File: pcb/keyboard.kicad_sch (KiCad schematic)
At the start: 21 parts, among them SW1 SW_Push, SW10 RotaryEncoder_Switch, SW2 SW_Push, SW3 SW_Push, SW4 SW_Push, SW5 SW_Push, SW6 SW_Push, SW7 SW_Push, SW8 SW_Push, SW9 SW_Push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

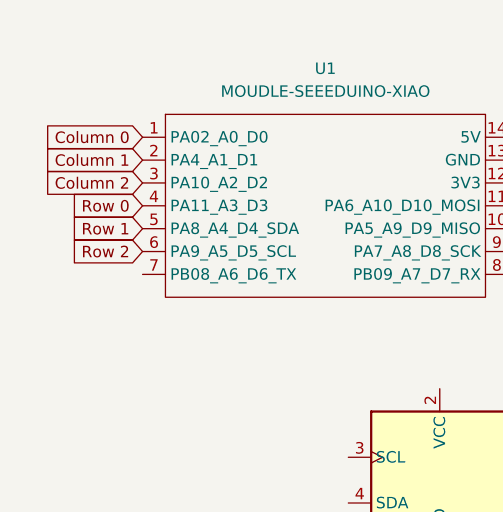
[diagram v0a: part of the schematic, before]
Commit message: connect switches to the microcontroller
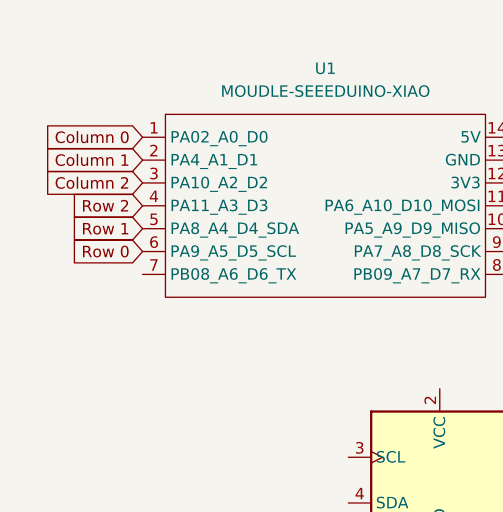
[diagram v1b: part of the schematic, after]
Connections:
- net Row 0: now also U1.6 (PA9_A5_D5_SCL); no longer U1.4 (PA11_A3_D3)
- net Row 2: now also U1.4 (PA11_A3_D3); no longer U1.6 (PA9_A5_D5_SCL)
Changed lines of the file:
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@@
 	(global_label "Row 2"
 		(shape input)
-		(at 30.48 50.8 180)
+		(at 30.48 45.72 180)
 		(fields_autoplaced yes)
 		(effects
@@
 		)
 		(property "Intersheetrefs" "${INTERSHEET_REFS}"
-			(at 21.5682 50.8 0)
+			(at 21.5682 45.72 0)
 			(hide yes)
 			(show_name no)
@@
 	(global_label "Row 0"
 		(shape input)
-		(at 30.48 45.72 180)
+		(at 30.48 50.8 180)
 		(fields_autoplaced yes)
 		(effects
@@
 		)
 		(property "Intersheetrefs" "${INTERSHEET_REFS}"
-			(at 21.5682 45.72 0)
+			(at 21.5682 50.8 0)
 			(hide yes)
 			(show_name no)

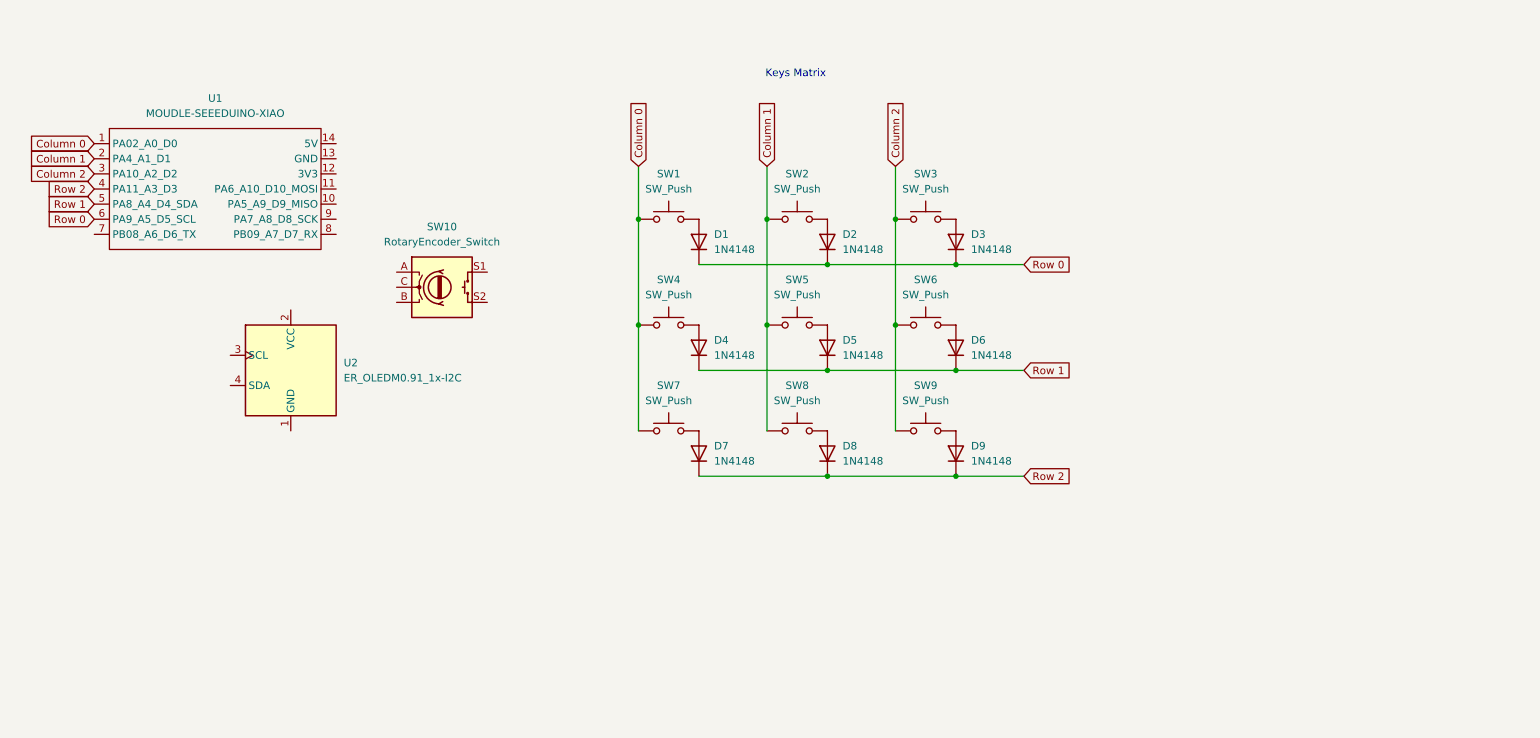
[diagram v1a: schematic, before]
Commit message: connect all components on schematic; remove invalid connections on pcb
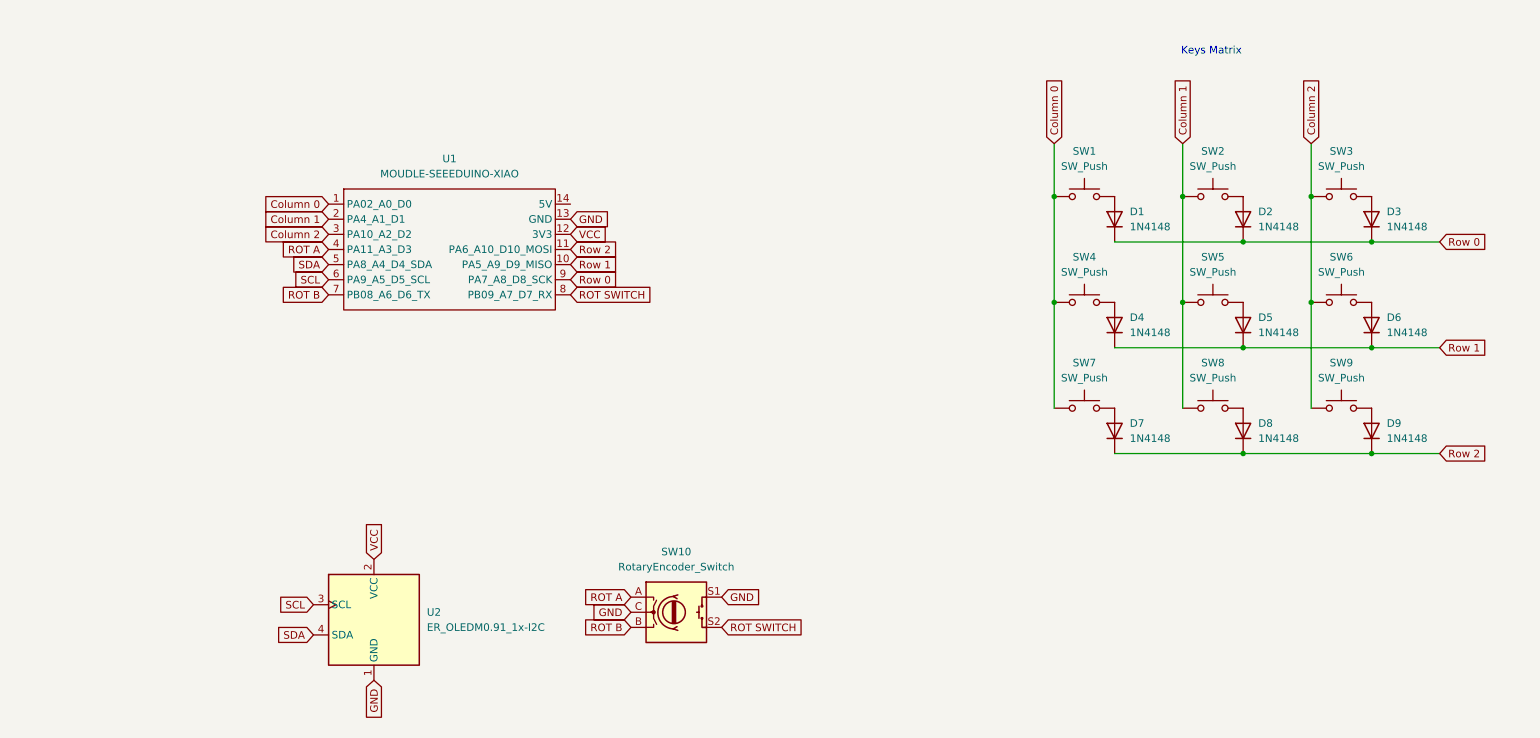
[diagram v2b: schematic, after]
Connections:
- net Row 0: now also U1.9 (PA7_A8_D8_SCK); no longer U1.6 (PA9_A5_D5_SCL)
- net Row 1: now also U1.10 (PA5_A9_D9_MISO); no longer U1.5 (PA8_A4_D4_SDA)
- net Row 2: now also U1.11 (PA6_A10_D10_MOSI); no longer U1.4 (PA11_A3_D3)
- net ROT A: now reaches SW10.A
- net ROT A: now also U1.4 (PA11_A3_D3)
- net ROT B: now reaches SW10.B
- net ROT B: now also U1.7 (PB08_A6_D6_TX)
- net GND: now reaches SW10.C
- net GND: now also SW10.S1, U1.13 (GND), U2.1 (GND)
- net ROT SWITCH: now reaches SW10.S2
- net ROT SWITCH: now also U1.8 (PB09_A7_D7_RX)
- net VCC: now reaches U2.2 (VCC)
- net VCC: now also U1.12 (3V3)
- net SCL: now reaches U2.3 (SCL)
- net SCL: now also U1.6 (PA9_A5_D5_SCL)
- net SDA: now reaches U2.4 (SDA)
- net SDA: now also U1.5 (PA8_A4_D4_SDA)
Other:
- moved on the sheet: D1, D2, D3, D4, D5, D6, D7, D8, D9, SW1, SW10, SW2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

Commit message: add rgb leds to schematic; update power labels; remove a switch and add rotary knob one to matrix instead
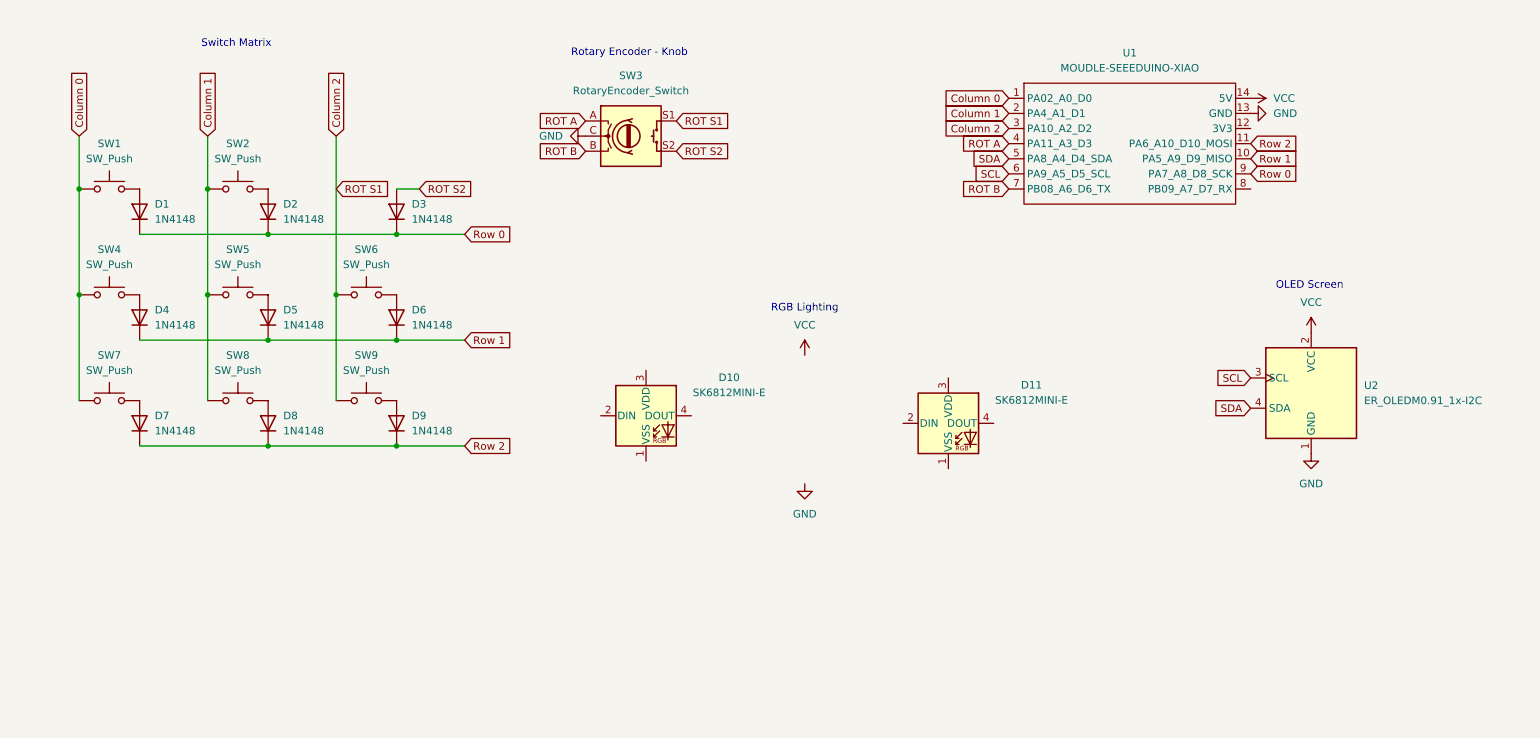
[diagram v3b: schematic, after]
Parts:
- removed SW3: SW_Push, Button_Switch_Keyboard:SW_Cherry_MX_1.00u_PCB, symbol Switch:SW_Push
- added D10, D11: SK6812MINI-E, footprints:SK6812MINI-E_fixed, symbol LED:SK6812MINI-E
- renumbered SW10 to SW3
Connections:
- net Column 2: now also SW3.S1
- net GND: no longer SW3.S1
- net VCC: now also U1.14 (5V); no longer U1.12 (3V3)
- net ROT S2: now reaches D3.2 (A)
- net ROT S2: now also SW3.S2
- net ROT SWITCH: no longer names the net of U1.8 (PB09_A7_D7_RX)
- net ROT SWITCH: no longer SW3.S2
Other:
- note added: "OLED Screen"
- note added: "RGB Lighting"
- note added: "Rotary Encoder - Knob"
- note added: "Switch Matrix"
- note removed: "Keys Matrix"
- moved on the sheet: D1, D2, D3, D4, D5, D6, D7, D8, D9, SW1, SW2, SW3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

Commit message: connect everything on the schematic
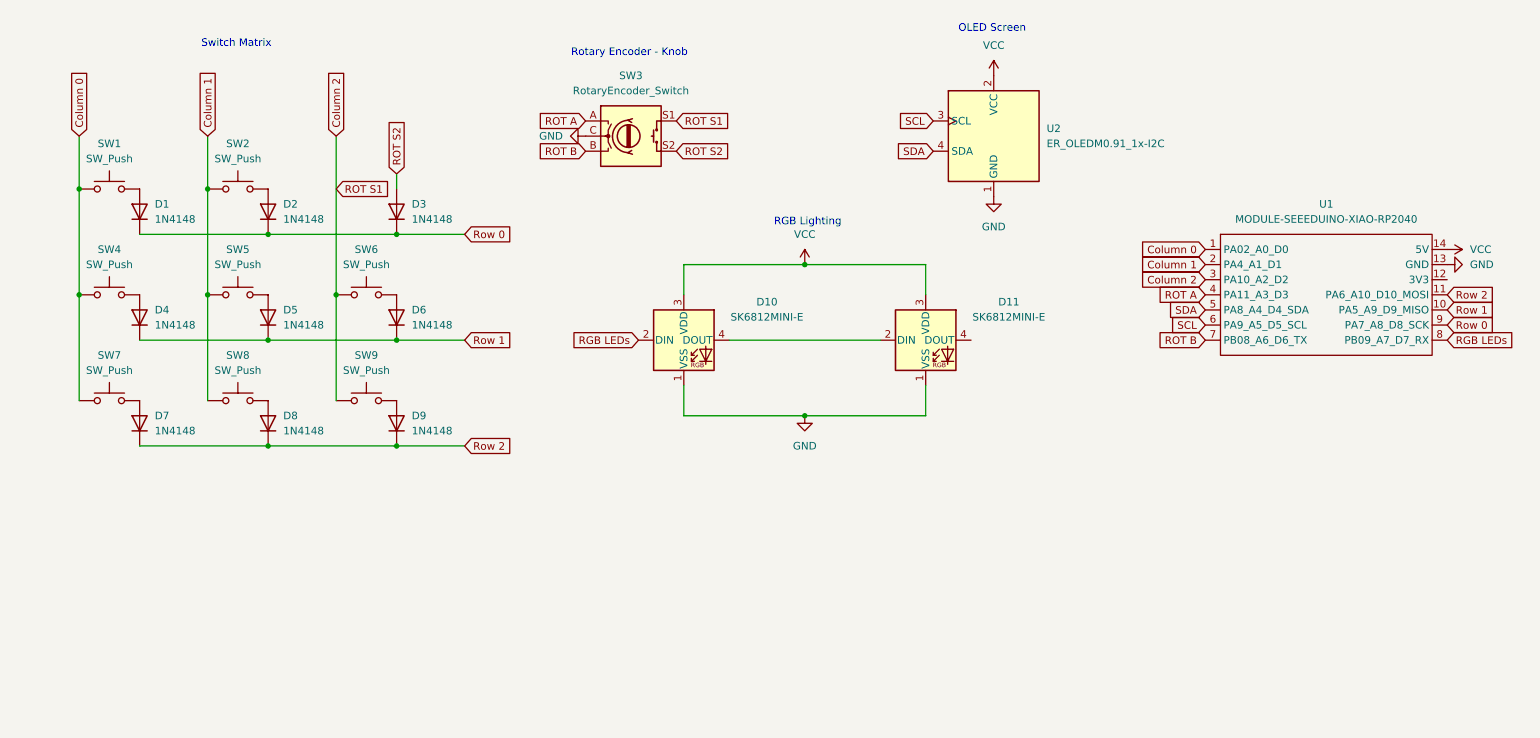
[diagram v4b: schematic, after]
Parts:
- U1: value MOUDLE-SEEEDUINO-XIAO -> MODULE-SEEEDUINO-XIAO-RP2040
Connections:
- net GND: now also D10.1 (VSS), D11.1 (VSS)
- net VCC: now also D10.3 (VDD), D11.3 (VDD)
- net RGB LEDs: now reaches U1.8 (PB09_A7_D7_RX)
- net RGB LEDs: now also D10.2 (DIN)
- net at D11.2 (DIN): now also D10.4 (DOUT)
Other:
- moved on the sheet: D10, D11, U1, U2

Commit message: make the board smaller, add third rgb
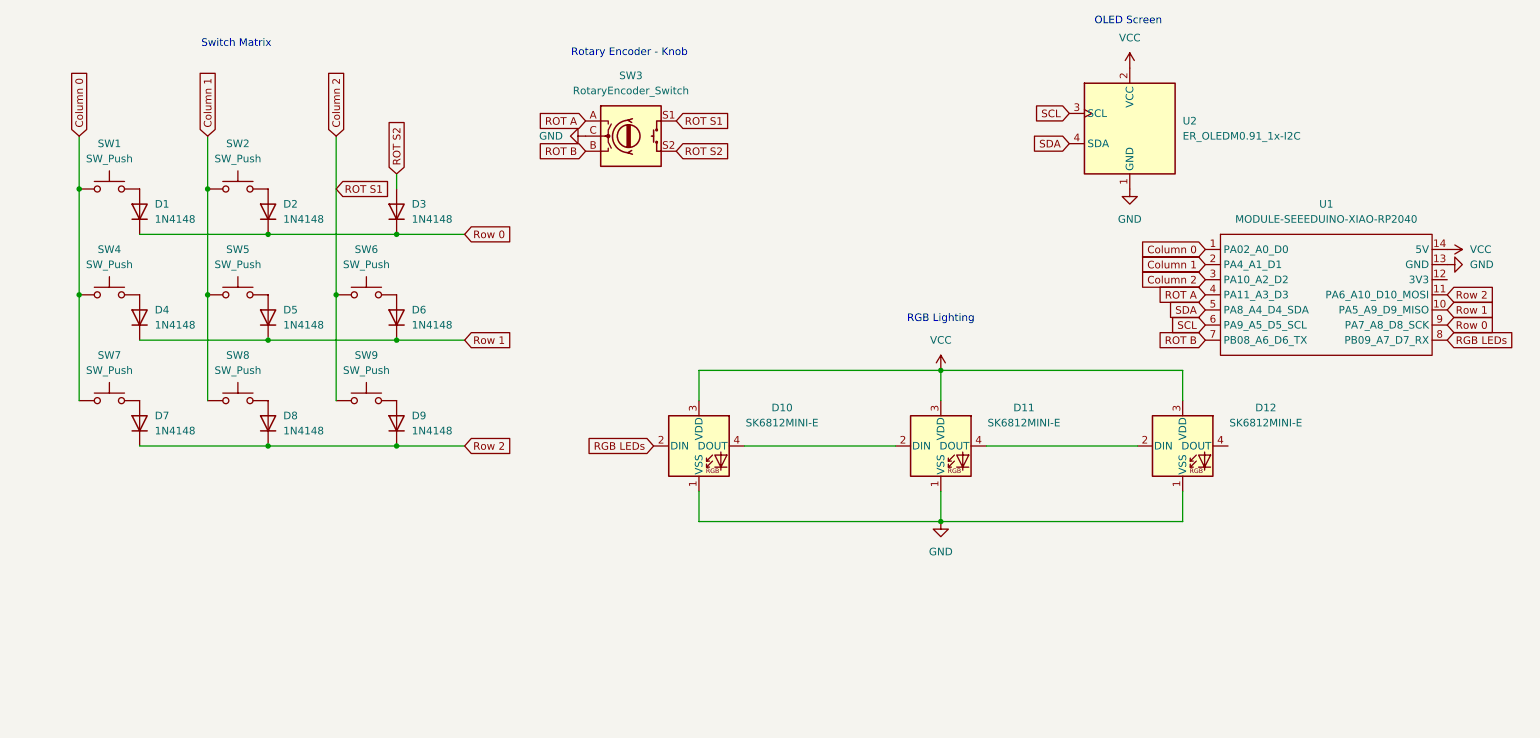
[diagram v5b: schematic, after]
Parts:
- added D12: SK6812MINI-E, footprints:SK6812MINI-E_fixed, symbol LED:SK6812MINI-E
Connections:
- net GND: now also D12.1 (VSS)
- net VCC: now also D12.3 (VDD)
- net at D11.4 (DOUT): now also D12.2 (DIN)
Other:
- moved on the sheet: D10, D11, U2
